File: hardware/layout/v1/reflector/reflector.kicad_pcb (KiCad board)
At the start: 4 copper layers, 24 x 24 mm, 7 parts, among them J1 Probe T-Header SMD

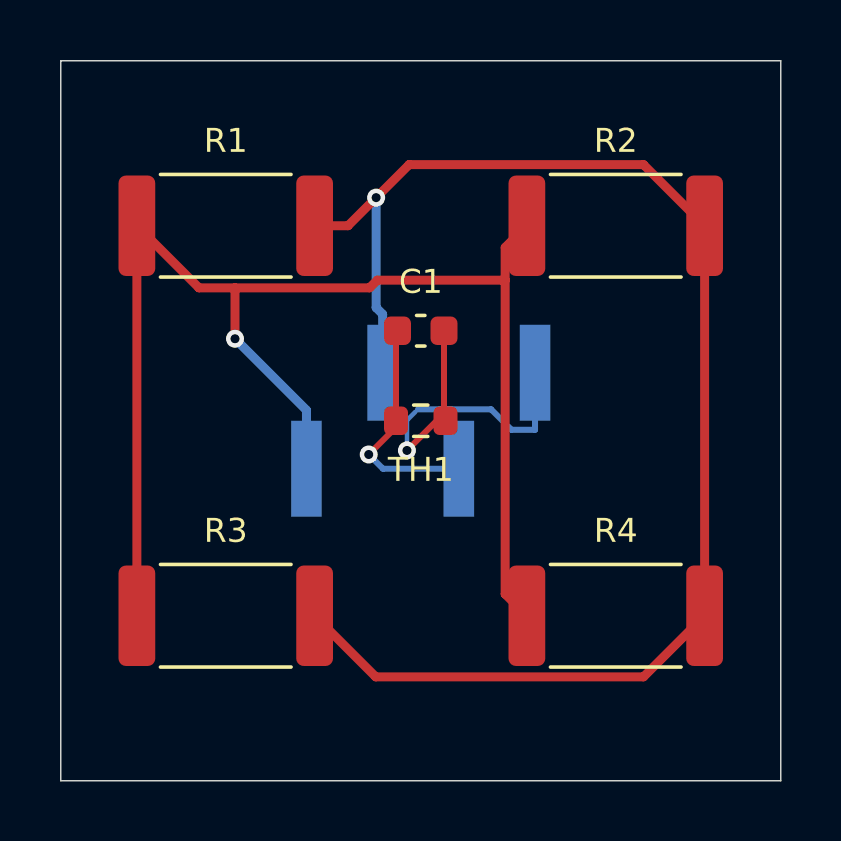
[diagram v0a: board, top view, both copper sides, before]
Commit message: Redesign crown PCB
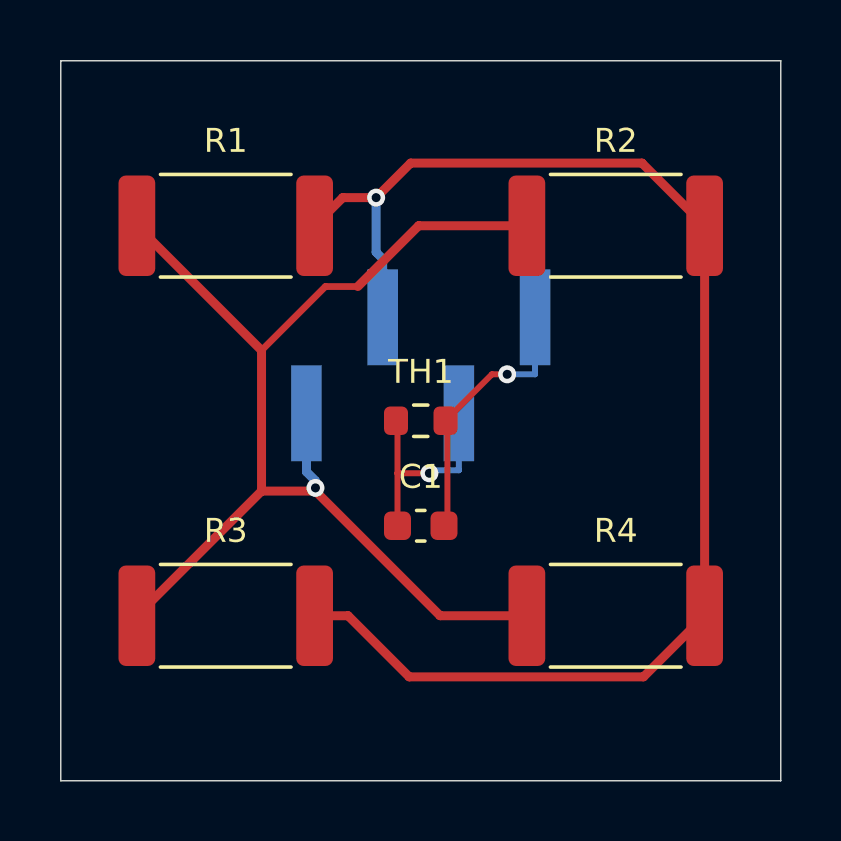
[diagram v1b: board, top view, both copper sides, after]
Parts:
- moved C1 6.50 mm to (12.0, -8.50)
- moved J1 1.85 mm to (12.0, -13.8)
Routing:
- net VIN_PROT: track 46.9 -> 40.3 mm
- net GND: track 11.8 -> 8.85 mm
- net HEAT_SW: track 48.3 -> 46.5 mm

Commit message: Add silkscreen connector labels to all PCB variants for improved assembly identification
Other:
- board text added: "PROBE"

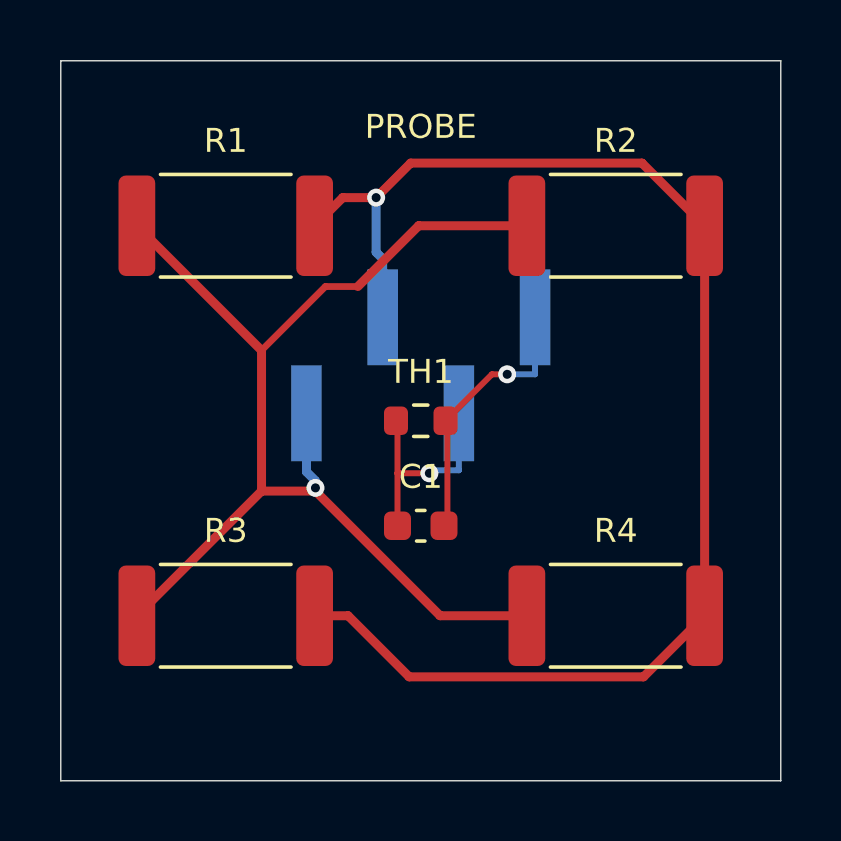
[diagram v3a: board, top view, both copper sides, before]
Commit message: Update enclosure dimensions, add power board, upgrade sensors, and redesign base bay for PMSA003I particulate module
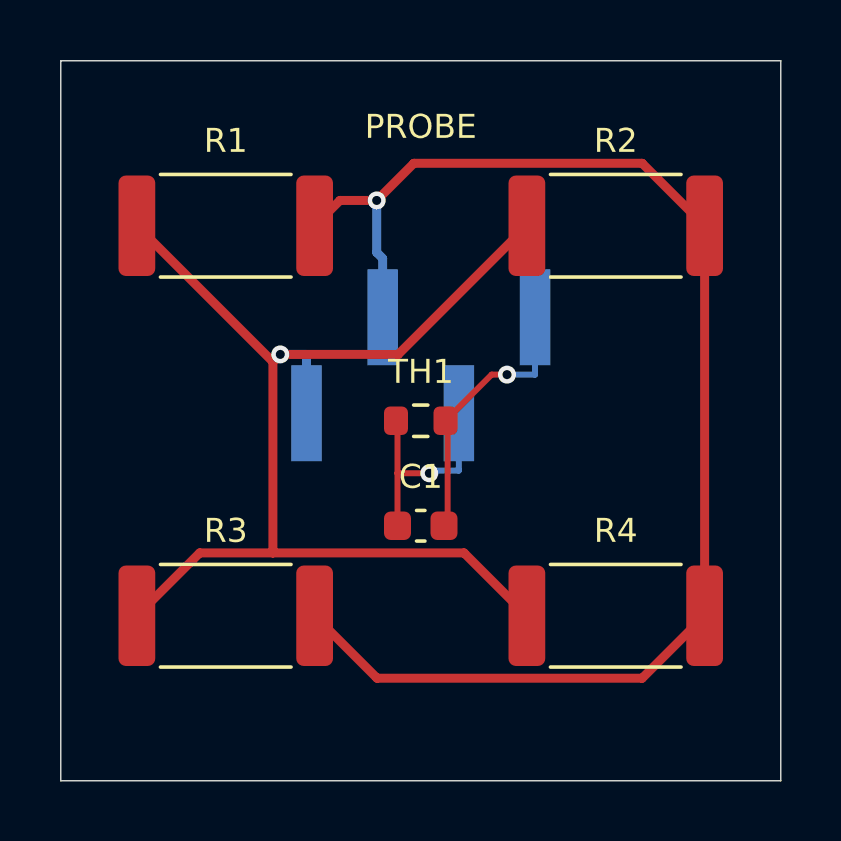
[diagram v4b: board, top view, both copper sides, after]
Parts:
- R1, R2, R3, R4: value 100R -> 27R
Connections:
- net VIN_PROT renamed +5V_HEAT

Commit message: Update documentation for 60V power system, STM32 crown board, 12V heaters, and expanded enclosure design
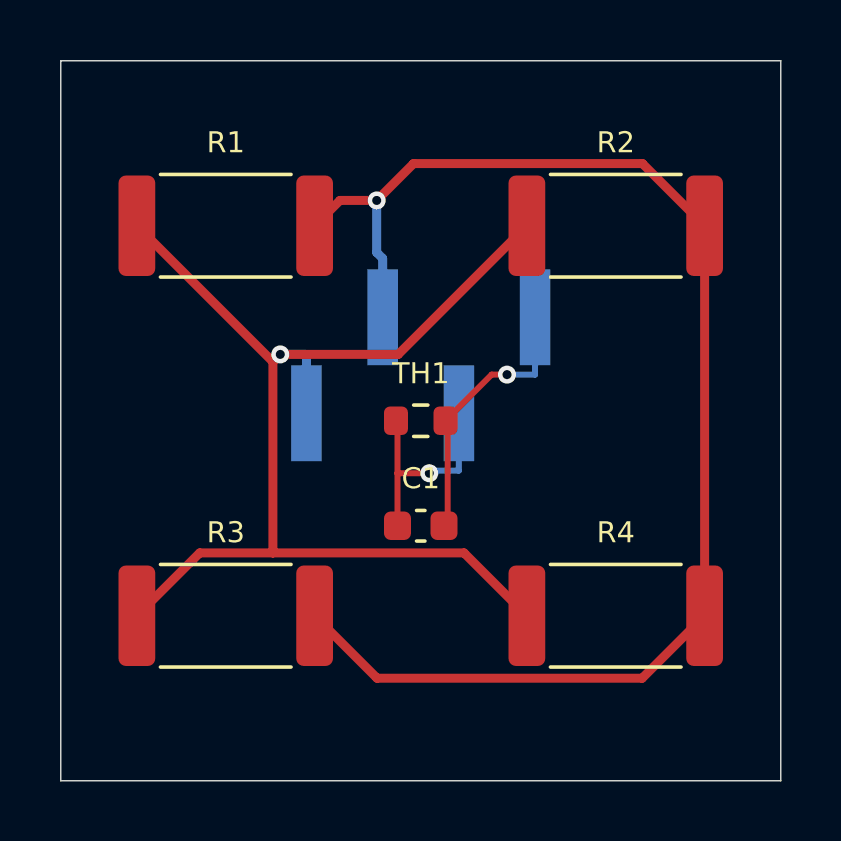
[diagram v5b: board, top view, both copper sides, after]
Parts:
- R1, R2, R3, R4: value 27R -> 120R
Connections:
- net +5V_HEAT renamed +12V_HEAT

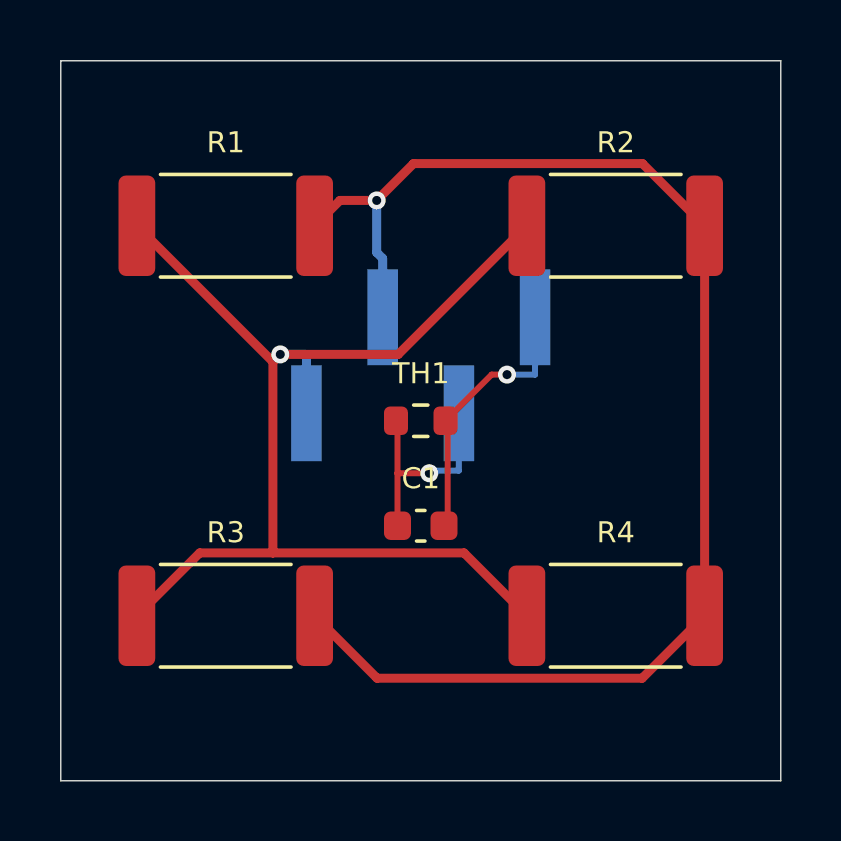
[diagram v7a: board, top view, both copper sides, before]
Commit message: Update enclosure dimensions to 236 mm height, replace JGS1 hemisphere with stock Ø 20×2 mm window, add optional crown_dome variant for horizon view, update all PCB thickness to 1.6 mm, and revise UV sensor positioning
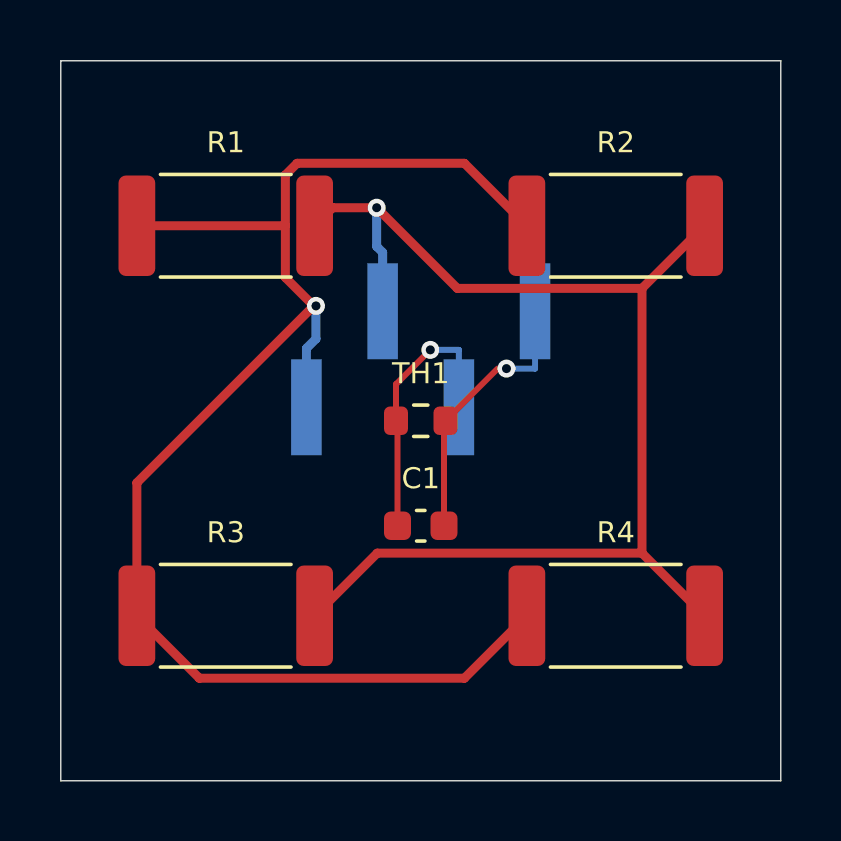
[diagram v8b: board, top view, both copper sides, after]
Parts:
- moved J1 0.20 mm to (12.0, -14.1)
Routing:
- net +12V_HEAT: track 40.7 -> 49.9 mm
- net HEAT_SW: track 46.4 -> 42.3 mm
- net NTC_SENSE: track 7.51 -> 9.22 mm
